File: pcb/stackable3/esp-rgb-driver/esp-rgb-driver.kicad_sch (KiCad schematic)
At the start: 48 parts, among them J0 DC-005, J1 JST PH, J2 JST PH, J3 JST SH, J5 STEMMA-Signal, J6 STEMMA-Signal, J8 Qwiic, Q1 ZC010DNG, Q2 ZC010DNG, Q3 ZC010DNG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

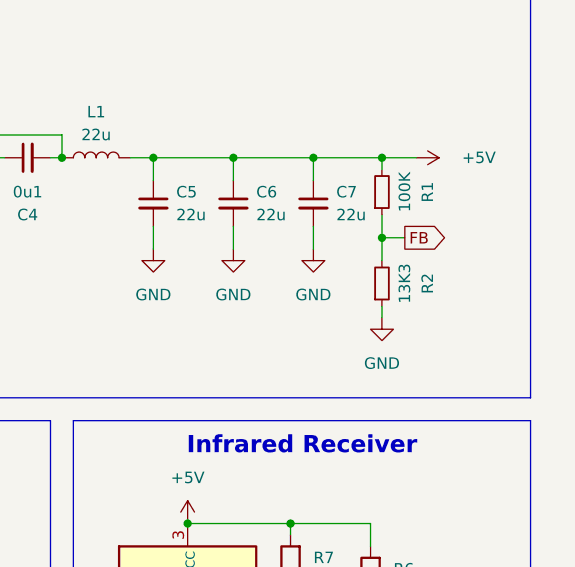
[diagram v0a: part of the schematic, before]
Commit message: Update R2 value, add LCSC part number on stackable3/esp-rgb-driver
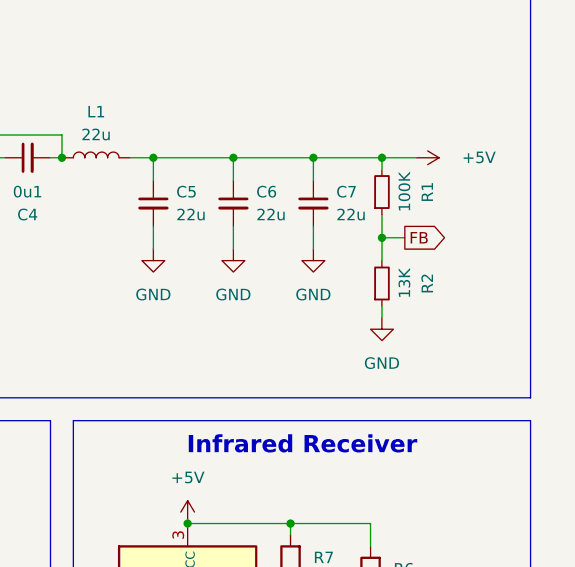
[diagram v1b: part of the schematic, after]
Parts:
- R2: value 13K3 -> 13K; LCSC Part (none) -> C22797
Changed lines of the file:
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@@
 			)
 		)
-		(property "Value" "13K3"
+		(property "Value" "13K"
 			(at 267.97 48.26 90)
 			(effects
@@
 			(effects
 				(font
+					(size 1.27 1.27)
+				)
+				(hide yes)
+			)
+		)
+		(property "LCSC Part" "C22797"
+			(at 265.43 48.26 90)
+			(effects
+				(font

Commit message: Rework stackable3/esp-rgb-driver as v3
- Add pull-up resistors to inverter inputs
- Add optional onboard 1x1 RGB LEDs for each output channel
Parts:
- removed J1, J2: JST PH, connector:JST_PH_S4B-PH-SM4-TB_1x04-1MP_P2.00mm_Horizontal, symbol Connector_Generic_MountingPin:Conn_01x04_MountingPin
- removed J5, J6: STEMMA-Signal, connector:STEMMA-Signal-SMD-horizontal, symbol connector:STEMMA-Signal
- removed JP1: Open, Jumper:SolderJumper-2_P1.3mm_Open_TrianglePad1.0x1.5mm, symbol Jumper:SolderJumper_2_Open
- removed Q1, Q2, Q3: ZC010DNG, package:PDFN-8_L3.2-W3.1-P0.65-LS3.4-BL-EP2, symbol discrete:ZC010DNG
- removed R5, R7: 10K, Resistor_SMD:R_0402_1005Metric, symbol Device:R
- removed SW5: 3.3mm, electromechanical:SW_Push_1P1T_NO_3.3x3.3mm_MP, symbol electromechanical:SW_Push_MountingPin
- removed U2, U6: SN74LVC1T45Z6, Package_TO_SOT_SMD:SOT-563, symbol ic:SN74LVC1T45Z6
- removed U3, U4: WS2811F, package:FSOP-8_3.3x1.7mm_P0.80mm, symbol ic:WS2811F
- removed U7, U8, U9: NC7WZ14P6X, package:SOT-363_SC-70-6_HandSolder, symbol ic:NC7WZ14P6X
- added C8: 0u1, discrete:C_0402_1005Metric, symbol Device:C_Small
- added C9: 1u, discrete:C_0402_1005Metric, symbol Device:C_Small
- added Q4: 2N7002DW, Package_TO_SOT_SMD:SOT-363_SC-70-6, symbol discrete:2N7002DW
- added R5, R8: 10R, Resistor_SMD:R_0402_1005Metric, symbol Device:R_Small
- added RN4: 10K, discrete:R_Array_Convex_4x0603, symbol Device:R_Pack04_Split
- added SR1: R020, Resistor_SMD:R_2512_6332Metric_Pad1.40x3.35mm_HandSolder, symbol Device:R
- added U2: INA226, Package_SO:VSSOP-10_3x3mm_P0.5mm, symbol Sensor_Energy:INA226
- C0: value 470u -> 100u; footprint Capacitor_SMD:CP_Elec_8x10 -> Capacitor_THT:CP_Radial_D6.3mm_P2.50mm
- J8: footprint connector:Qwiic-SMD-horizontal-logo-bottom-pinout -> connector:Qwiic-SMD-horizontal-logo
- L1: footprint discrete:L_Power_7.0x6.6mm_0630 -> discrete:L_1008_2520Metric
- RN1: footprint discrete:R_Array_Convex_4x0603_HandSolder -> discrete:R_Array_Convex_4x0603; LCSC Part C110924 -> (none)
- SM1: footprint module:ESP32-C3-Super-Mini-Castellated-SMD -> module:ESP32-C3-Super-Mini-Castellated-SMD-only
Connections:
- net +3V3: now also C9.1, Q4.2 (G), Q4.5 (G), RN4.5 (R4.2), RN4.6 (R3.2), RN4.7 (R2.2), RN4.8 (R1.2), U2.6 (VS); no longer RN1.5 (R4.2), RN1.7 (R2.2)
- net +5V: now also RN1.5 (R4.2), RN1.7 (R2.2)
- net BUTTON: now also SM1.1 (ADC/GPIO1), RN4.1 (R1.1); no longer SM1.21 (GPIO21/TX)
- net BUTTON_SM_1: now also SM1.10 (GPIO10), RN4.2 (R2.1); no longer RN1.2 (R2.1), SM1.1 (ADC/GPIO1)
- net BUTTON_SM_2: now also SM1.20 (GPIO20/RX), RN4.3 (R3.1); no longer RN1.3 (R3.1), SM1.10 (GPIO10)
- net BUTTON_SM_3: now also SM1.21 (GPIO21/TX), RN4.4 (R4.1); no longer RN1.1 (R1.1), SM1.0 (ADC/GPIO0)
- net GND: now also J0.3, C9.2, U2.1 (A1), U2.2 (A0), U2.7 (GND)
- net IR_RX: now also RN1.4 (R4.1), Q4.6 (D)
- net IR_RX_3V3: now also RN1.3 (R3.1), Q4.1 (S)
- net PIXEL_DATA_3V3: now also RN1.1 (R1.1), Q4.4 (S)
- net SCL: now also U2.5 (SCL)
- net SDA: now also U2.4 (SDA)
- net 24V_RAW renamed 24V_SHUNT
- net 24V_SHUNT: now also R8.1, SR1.2; no longer J0.1
- removed net BUTTON_SM_4: RN1.4 (R4.1), SM1.20 (GPIO20/RX)
- new net DC_IN_RAW: J0.1, R5.1, SR1.1
- new net PIXEL_DATA: Q4.3 (D), RN1.2 (R2.1)
- new net RGB_LED_EN: SM1.0 (ADC/GPIO0)
- new net VIN_SENSE+: C8.1, R5.2, U2.10 (Vin+)
- new net VIN_SENSE-: C8.2, R8.2, U2.8 (Vbus), U2.9 (Vin-)
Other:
- added sheet RGB (rgb.kicad_sch)
- moved on the sheet: J3, J8, LED3, R6, U5

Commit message: Add project info to stackable3/esp-rgb-driver
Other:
- title: (none) -> ESPHome 24v RGB LED strip driver
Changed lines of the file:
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@@
 	(generator_version "8.0")
 	(paper "A4")
+	(title_block
+		(title "ESPHome 24v RGB LED strip driver")
+		(date "2025-03-18")
+		(rev "v3")
+	)
 	(junction
 		(at 257.81 78.74)

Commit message: Add LCSC part numbers to stackable3/esp-rgb-driver
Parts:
- C0: LCSC Part C7471889 -> C5379947
- C1, C2: LCSC Part (none) -> C22367825
- C3, C4: LCSC Part (none) -> C152814
- C5, C6, C7: LCSC Part (none) -> C86295
- C9: LCSC Part (none) -> C52923
- L1: LCSC Part (none) -> C5832391
- LED1: LCSC Part (none) -> C7496823
- LED2: LCSC Part (none) -> C779449
- R1: LCSC Part (none) -> C25803
- R3, R6: LCSC Part (none) -> C25905
- R4: LCSC Part (none) -> C11702
- RN1: LCSC Part (none) -> C110924
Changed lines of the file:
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@@
 			)
 		)
+		(property "LCSC Part" "C110924"
+			(at 69.85 77.47 0)
+			(effects
+				(font
+					(size 1.27 1.27)
+				)
+				(hide yes)
+			)
+		)
 		(pin "4"
 		)
@@
 			)
 		)
+		(property "LCSC Part" "C86295"
+			(at 248.92 39.37 0)
+			(effects
+				(font
+					(size 1.27 1.27)
+				)
+				(hide yes)
+			)
+		)
 		(pin "1"
 		)
@@
 			)
 		)
+		(property "LCSC Part" "C25905"
+			(at 68.58 137.16 0)
+			(effects
+				(font
+					(size 1.27 1.27)
+				)
+				(hide yes)
+			)
+		)
 		(pin "1"
 		)
@@
 			)
 		)
-		(property "LCSC Part" ""
+		(property "LCSC Part" "C52923"
 			(at 185.42 96.52 0)
 			(effects
@@
 			)
 		)
+		(property "LCSC Part" "C7496823"
+			(at 86.36 58.42 0)
+			(effects
+				(font
+					(size 1.27 1.27)
+				)
+				(hide yes)
+			)
+		)
 		(pin "2"
 		)
@@
 			)
 		)
-		(property "LCSC Part" ""
+		(property "LCSC Part" "C5832391"
 			(at 233.68 34.29 90)
 			(effects
@@
 			)
 		)
+		(property "LCSC Part" "C779449"
+			(at 158.75 41.91 0)
+			(effects
+				(font
+					(size 1.27 1.27)
+				)
+				(hide yes)
+			)
+		)
 		(pin "1"
 		)
@@
 			)
 		)
+		(property "LCSC Part" ""
+			(at 68.58 146.05 90)
+			(effects
+				(font
+					(size 1.27 1.27)
+				)
+				(hide yes)
+			)
+		)
 		(pin "2"
 		)
@@
 			)
 		)
+		(property "LCSC Part" "C22367825"
+			(at 181.61 36.83 0)
+			(effects
+				(font
+					(size 1.27 1.27)
+				)
+				(hide yes)
+			)
+		)
 		(pin "1"
 		)
@@
 			)
 		)
+		(property "LCSC Part" "C22367825"
+			(at 172.72 36.83 0)
+			(effects
+				(font
+					(size 1.27 1.27)
+				)
+				(hide yes)
+			)
+		)
 		(pin "1"
 		)
@@
 			)
 		)
+		(property "LCSC Part" "C25803"
+			(at 265.43 38.1 90)
+			(effects
+				(font
+					(size 1.27 1.27)
+				)
+				(hide yes)
+			)
+		)
 		(pin "2"
 		)
@@
 			)
 		)
+		(property "LCSC Part" "C110924"
+			(at 50.8 77.47 0)
+			(effects
+				(font
+					(size 1.27 1.27)
+				)
+				(hide yes)
+			)
+		)
 		(pin "4"
 		)
@@
 			)
 		)
+		(property "LCSC Part" "C110924"
+			(at 52.07 99.06 0)
+			(effects
+				(font
+					(size 1.27 1.27)
+				)
+				(hide yes)
+			)
+		)
 		(pin "4"
 		)
@@
 			)
 		)
+		(property "LCSC Part" "C152814"
+			(at 226.06 34.29 90)
+			(effects
+				(font
+					(size 1.27 1.27)
+				)
+				(hide yes)
+			)
+		)
 		(pin "1"
 		)
@@
 			)
 		)
+		(property "LCSC Part" "C86295"
+			(at 240.03 39.37 0)
+			(effects
+				(font
+					(size 1.27 1.27)
+				)
+				(hide yes)
+			)
+		)
 		(pin "1"
 		)
@@
 			)
 		)
+		(property "LCSC Part" "C11702"
+			(at 151.13 41.91 90)
+			(effects
+				(font
+					(size 1.27 1.27)
+				)
+				(hide yes)
+			)
+		)
 		(pin "1"
 		)
@@
 			)
 		)
+		(property "LCSC Part" "C110924"
+			(at 59.69 135.89 0)
+			(effects
+				(font
+					(size 1.27 1.27)
+				)
+				(hide yes)
+			)
+		)
 		(pin "4"
 		)
@@
 			)
 		)
+		(property "LCSC Part" "C152814"
+			(at 190.5 36.83 0)
+			(effects
+				(font
+					(size 1.27 1.27)
+				)
+				(hide yes)
+			)
+		)
 		(pin "1"
 		)
@@
 			)
 		)
-		(property "LCSC Part" "C7471889"
+		(property "LCSC Part" "C5379947"
 			(at 137.16 35.56 0)
 			(effects
@@
 			)
 		)
+		(property "LCSC Part" "C86295"
+			(at 257.81 39.37 0)
+			(effects
+				(font
+					(size 1.27 1.27)
+				)
+				(hide yes)
+			)
+		)
 		(pin "1"
 		)
@@
 			(effects
 				(font
+					(size 1.27 1.27)
+				)
+				(hide yes)
+			)
+		)
+		(property "LCSC Part" "C25905"
+			(at 78.74 58.42 90)
+			(effects
+				(font
